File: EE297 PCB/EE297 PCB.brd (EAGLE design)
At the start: 293.4 x 116.8 mm, 98 parts, among them IC1 MEGA32-P, IC2 MEGA32-P, IC3 7805T, K1 CQ1-12V, K3 CQ1-12V, T1 BC547, T2 TIP122, T3 TIP122, T4 TIP122, T5 BC547

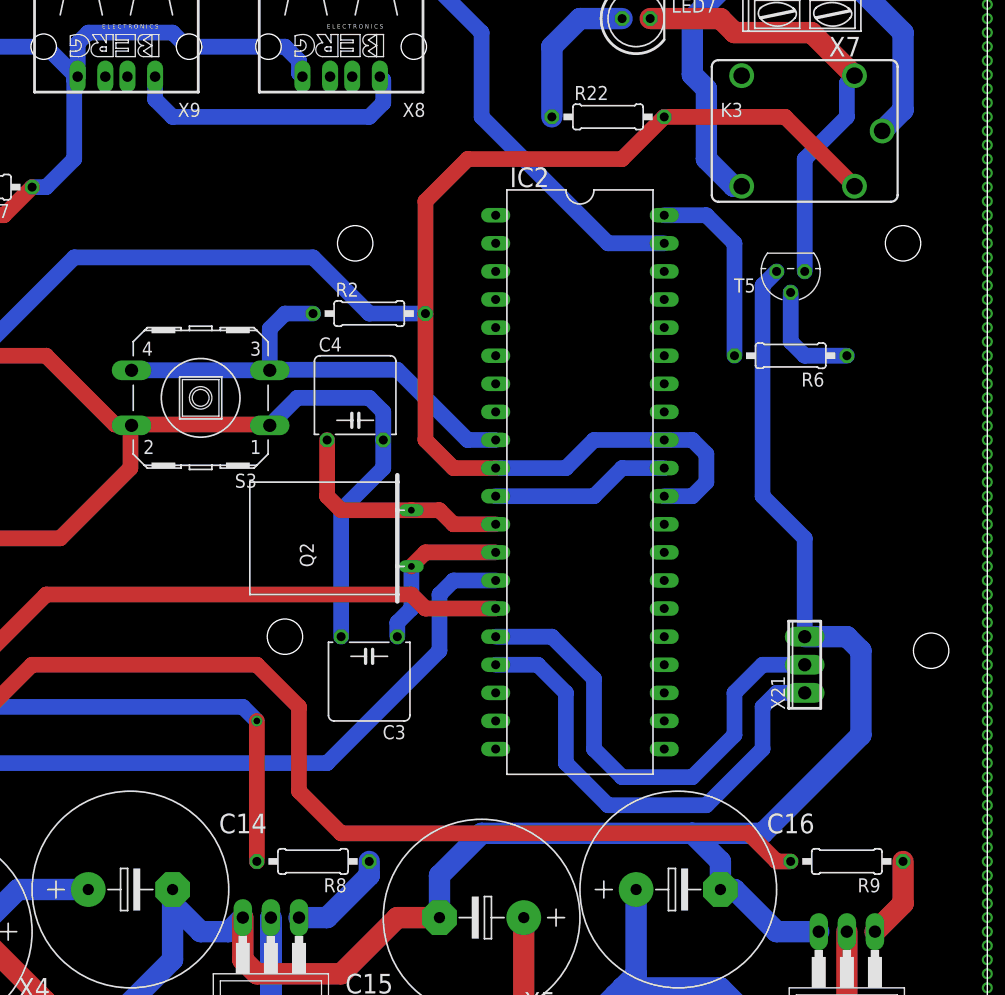
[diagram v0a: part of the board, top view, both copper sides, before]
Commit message: MS Project PCB Design Added
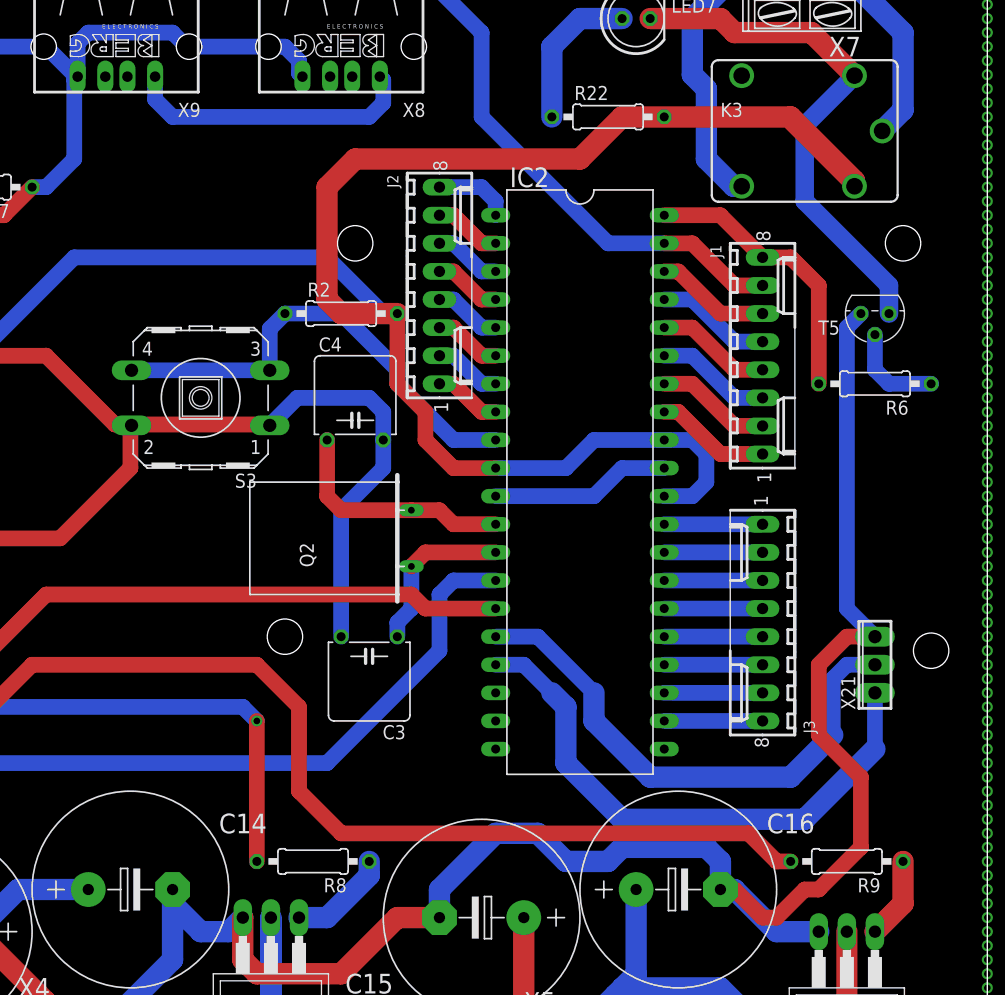
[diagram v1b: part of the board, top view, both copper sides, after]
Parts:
- added J1, J2, J3: 22-27-2081-08, con-molex:6410-08
- moved T5 8.52 mm to (109.2, 77.5)
- moved R6 8.03 mm to (109.2, 71.1)
- moved X21 6.35 mm to (109.2, 45.7)
- moved R2 2.54 mm to (61.0, 77.5)
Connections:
- new net N$157: IC2.33, J1.1
- new net N$158: IC2.34, J1.2
- new net N$159: IC2.35, J1.3
- new net N$160: IC2.36, J1.4
- new net N$161: IC2.37, J1.5
- new net N$162: IC2.38, J1.6
- new net N$164: IC2.8, J2.1
- new net N$165: IC2.7, J2.2
- new net N$166: IC2.6, J2.3
- new net N$167: IC2.5, J2.4
- new net N$168: IC2.4, J2.5
- new net N$169: IC2.3, J2.6
- new net N$170: IC2.2, J2.7
- new net N$171: IC2.1, J2.8
- new net N$172: IC2.29, J3.1
- new net N$173: IC2.28, J3.2
- new net N$174: IC2.27, J3.3
- new net N$175: IC2.26, J3.4
- new net N$176: IC2.25, J3.5
- new net N$177: IC2.24, J3.6
- new net N$178: IC2.23, J3.7
- new net N$179: IC2.22, J3.8
- net N$44: now also J1.8
- net N$45: now also J1.7
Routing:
- net VCC: track 558.3 -> 592.1 mm
- net N$45: track 208.5 -> 219.0 mm
- net N$162: track 0.00 -> 10.5 mm
- net N$160: track 0.00 -> 10.5 mm
- net N$159: track 0.00 -> 10.5 mm
- net N$158: track 0.00 -> 10.5 mm
- net N$157: track 0.00 -> 10.5 mm
- net N$161: track 0.00 -> 10.5 mm
- net N$179: track 0.00 -> 8.89 mm
- net N$178: track 0.00 -> 8.89 mm
- net N$177: track 0.00 -> 8.89 mm
- net N$176: track 0.00 -> 8.89 mm
- net N$175: track 0.00 -> 8.89 mm
- net N$174: track 0.00 -> 8.89 mm
- net N$173: track 0.00 -> 8.89 mm
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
